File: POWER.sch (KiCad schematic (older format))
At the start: 42 parts, among them J6001 BATT1, J6002 BATT2_XT60, J6003 BATT2_JST, J6004 BATT4_CELL2, J6005 BATT4_CELL1, J6006 BATT5_CELL2, J6007 BATT5_CELL1, J6008 BATT3_JST, U6001 D24V50F5, U6002 D36V28F3, U6003 LM7809_TO220, U6004 D36V50F6, U6005 D36V50F6, U6006 D24V50F5

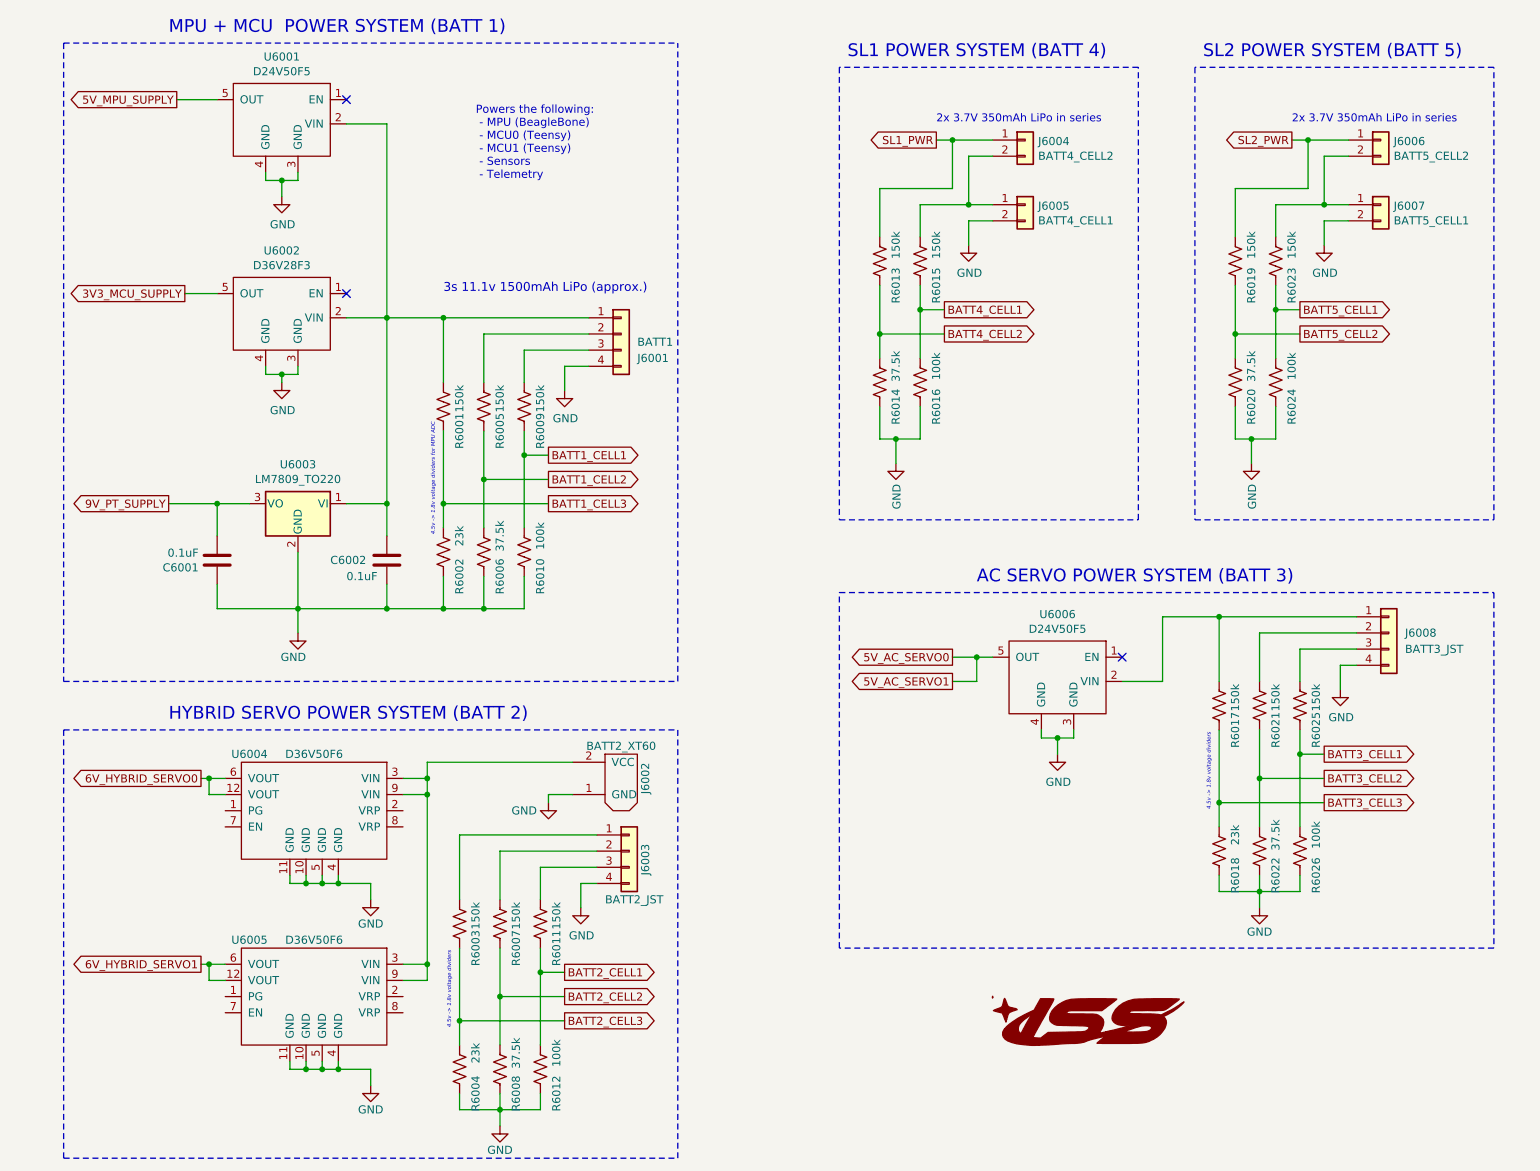
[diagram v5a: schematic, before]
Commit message: Fixed D36V28F3 footprint, made a Telemetrum footprint and symbol
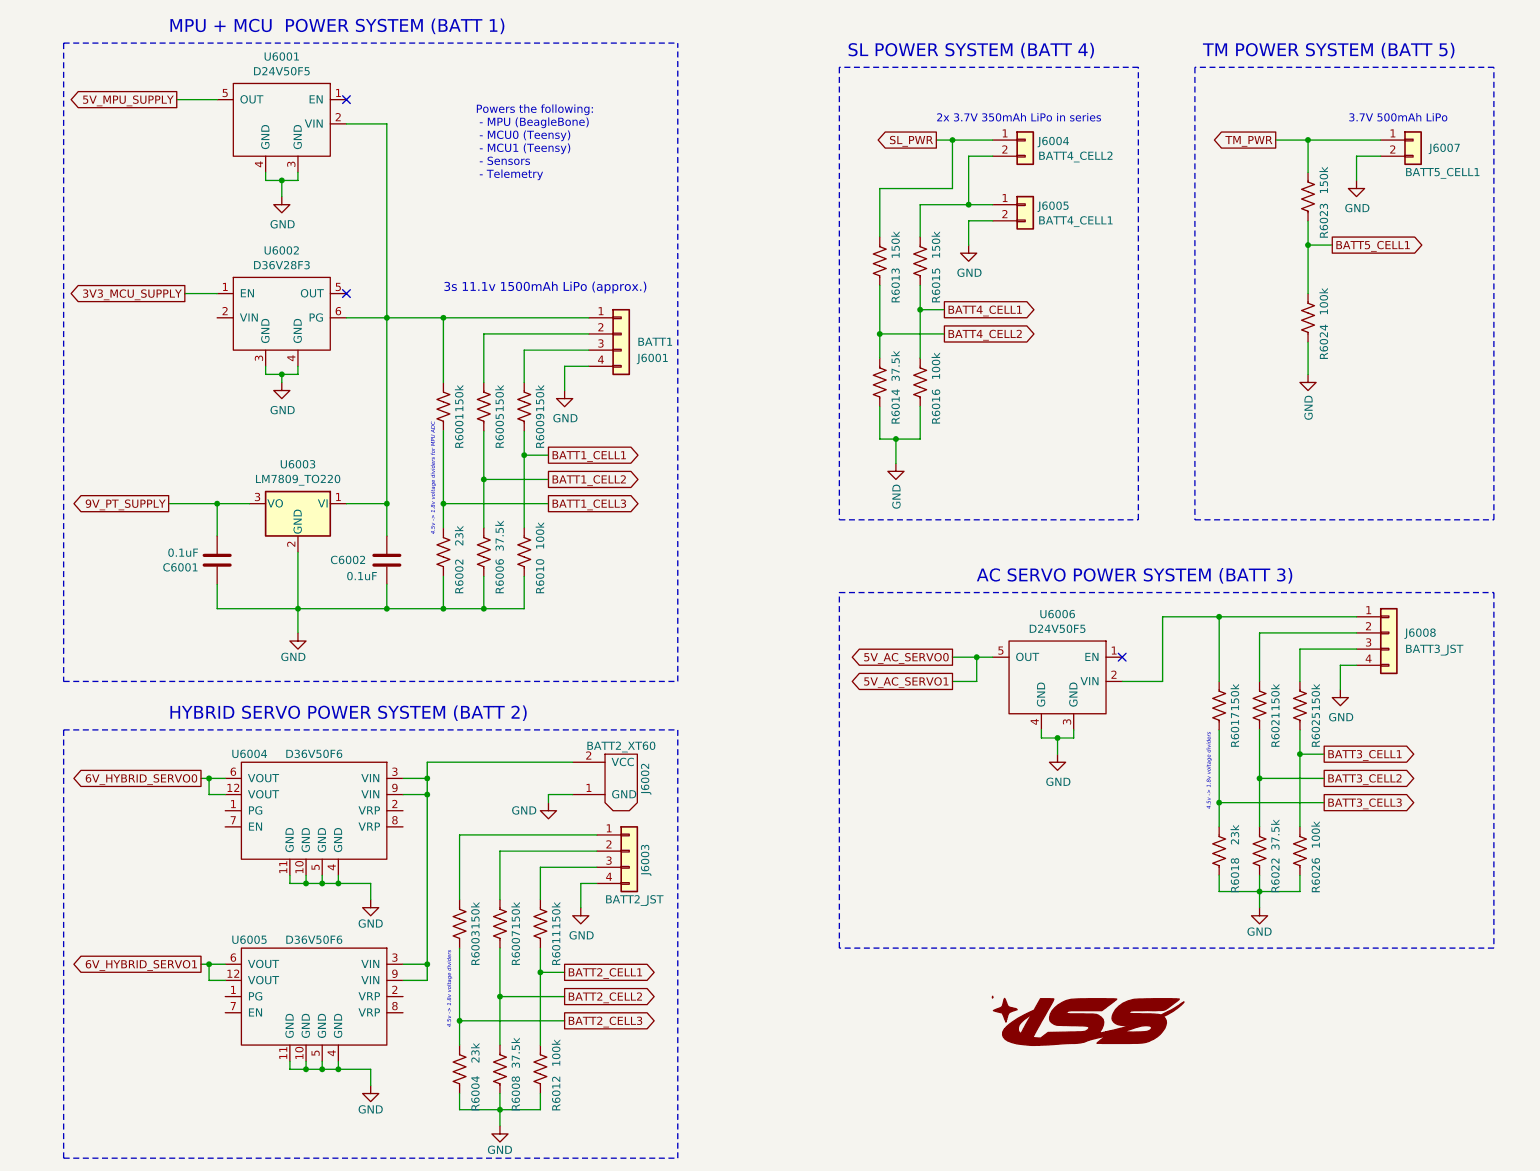
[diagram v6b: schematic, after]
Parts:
- removed J6006: BATT5_CELL2, Connector_JST:JST_PH_B2B-PH-K_1x02_P2.00mm_Vertical, symbol Connector_Generic:Conn_01x02
- removed R6019: 150k, symbol D24V50F5:R_US
- removed R6020: 37.5k, symbol D24V50F5:R_US
- removed U6002: D36V28F3, D24V50F5:D24V50F5, symbol D24V50F5:D24V50F5
- added U6002: D36V28F3, D36V28F3:D36V28F3, symbol D36V28F3:D36V28F3
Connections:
- net 3V3_MCU_SUPPLY: now also U6002.1 (EN)
- net GND: now also U6002.3 (GND), U6002.4 (GND)
- net at C6002.1, J6001.1 (Pin_1), R6001.2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: now also U6002.6 (PG)
- net TM_PWR: now reaches J6007.1 (Pin_1), R6023.2
- net SL1_PWR renamed SL_PWR
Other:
- note added: "3.7V 500mAh LiPo"
- note added: "SL POWER SYSTEM (BATT 4)"
- note added: "TM POWER SYSTEM (BATT 5)"
- note removed: "SL1 POWER SYSTEM (BATT 4)"
- note removed: "SL2 POWER SYSTEM (BATT 5)"
- moved on the sheet: J6007, R6023, R6024
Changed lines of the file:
@@
 	7900 3700 7900 900
-$Comp
-L Connector_Generic:Conn_01x02 J6007
-U 1 1 5FF794E5
-P 9400 1750
-F 0 "J6007" H 9480 1742 50  0000 L CNN
-F 1 "BATT5_CELL1" H 9480 1651 50  0000 L CNN
-F 2 "Connector_JST:JST_PH_B2B-PH-K_1x02_P2.00mm_Vertical" H 9400 1750 50  0001 C CNN
-F 3 "~" H 9400 1750 50  0001 C CNN
-	1    9400 1750
-	1    0    0    -1
-$EndComp
-$Comp
-L Connector_Generic:Conn_01x02 J6006
-U 1 1 5FF794EB
-P 9400 1350
-F 0 "J6006" H 9480 1342 50  0000 L CNN
-F 1 "BATT5_CELL2" H 9480 1251 50  0000 L CNN
-F 2 "Connector_JST:JST_PH_B2B-PH-K_1x02_P2.00mm_Vertical" H 9400 1350 50  0001 C CNN
-F 3 "~" H 9400 1350 50  0001 C CNN
-	1    9400 1350
-	1    0    0    -1
-$EndComp
 $Comp
 L power:GND #PWR06015
 U 1 1 5FF794F1
-P 9050 2000
-F 0 "#PWR06015" H 9050 1750 50  0001 C CNN
-F 1 "GND" H 9055 1827 50  0000 C CNN
-F 2 "" H 9050 2000 50  0001 C CNN
-F 3 "" H 9050 2000 50  0001 C CNN
-	1    9050 2000
-	1    0    0    -1
-$EndComp
-Wire Wire Line
-	9200 1450 9050 1450
-Wire Wire Line
-	9200 1850 9050 1850
-Wire Wire Line
-	9050 2000 9050 1850
-Text GLabel 8900 2400 2    50   Output ~ 0
+P 9250 1600
+F 0 "#PWR06015" H 9250 1350 50  0001 C CNN
+F 1 "GND" H 9255 1427 50  0000 C CNN
+F 2 "" H 9250 1600 50  0001 C CNN
+F 3 "" H 9250 1600 50  0001 C CNN
+	1    9250 1600
+	1    0    0    -1
+$EndComp
+Wire Wire Line
+	9400 1450 9250 1450
+Wire Wire Line
+	9250 1600 9250 1450
+Text GLabel 9100 2000 2    50   Output ~ 0
 BATT5_CELL1
-Text GLabel 8900 2550 2    50   Output ~ 0
-BATT5_CELL2
 $Comp
 L D24V50F5:R_US R6023
 U 1 1 5FF794FD
-P 8750 2100
-F 0 "R6023" V 8650 2250 50  0000 C CNN
-F 1 "150k" V 8650 2000 50  0000 C CNN
-F 2 "" V 8790 2090 50  0001 C CNN
-F 3 "~" H 8750 2100 50  0001 C CNN
-	1    8750 2100
-	-1   0    0    1
-$EndComp
-$Comp
-L D24V50F5:R_US R6019
-U 1 1 5FF79503
-P 8500 2100
-F 0 "R6019" V 8400 2250 50  0000 C CNN
-F 1 "150k" V 8400 2000 50  0000 C CNN
-F 2 "" V 8540 2090 50  0001 C CNN
-F 3 "~" H 8500 2100 50  0001 C CNN
-	1    8500 2100
-	-1   0    0    1
-$EndComp
-Wire Wire Line
-	8750 1950 8750 1750
-Wire Wire Line
-	8750 2250 8750 2400
-Wire Wire Line
-	8750 2400 8900 2400
-Wire Wire Line
-	8500 2250 8500 2550
-Wire Wire Line
-	8500 2550 8900 2550
+P 8950 1700
+F 0 "R6023" V 8850 1850 50  0000 C CNN
+F 1 "150k" V 8850 1600 50  0000 C CNN
+F 2 "" V 8990 1690 50  0001 C CNN
+F 3 "~" H 8950 1700 50  0001 C CNN
+	1    8950 1700
+	-1   0    0    1
+$EndComp
+Wire Wire Line
+	8950 1550 8950 1350
+Wire Wire Line
+	8950 1850 8950 2000
+Wire Wire Line
+	8950 2000 9100 2000
 $Comp
 L D24V50F5:R_US R6024
 U 1 1 5FF7950E
-P 8750 2850
-F 0 "R6024" V 8650 3000 50  0000 C CNN
-F 1 "100k" V 8650 2750 50  0000 C CNN
-F 2 "" V 8790 2840 50  0001 C CNN
-F 3 "~" H 8750 2850 50  0001 C CNN
-	1    8750 2850
-	-1   0    0    1
-$EndComp
-$Comp
-L D24V50F5:R_US R6020
-U 1 1 5FF79514
-P 8500 2850
-F 0 "R6020" V 8400 3000 50  0000 C CNN
-F 1 "37.5k" V 8400 2750 50  0000 C CNN
-F 2 "" V 8540 2840 50  0001 C CNN
-F 3 "~" H 8500 2850 50  0001 C CNN
-	1    8500 2850
-	-1   0    0    1
-$EndComp
-Wire Wire Line
-	8750 3200 8750 3000
-Wire Wire Line
-	8500 3000 8500 3200
-Wire Wire Line
-	8500 3200 8600 3200
-Wire Wire Line
-	8750 1750 9050 1750
-Wire Wire Line
-	9050 1750 9050 1450
-Connection ~ 9050 1750
-Wire Wire Line
-	9050 1750 9200 1750
-Wire Wire Line
-	8600 3200 8600 3350
+P 8950 2450
+F 0 "R6024" V 8850 2600 50  0000 C CNN
+F 1 "100k" V 8850 2350 50  0000 C CNN
+F 2 "" V 8990 2440 50  0001 C CNN
+F 3 "~" H 8950 2450 50  0001 C CNN
+	1    8950 2450
+	-1   0    0    1
+$EndComp
+Wire Wire Line
+	8950 2800 8950 2600
 $Comp
 L power:GND #PWR06013
 U 1 1 5FF79524
-P 8600 3350
-F 0 "#PWR06013" H 8600 3100 50  0001 C CNN
-F 1 "GND" V 8605 3222 50  0000 R CNN
-F 2 "" H 8600 3350 50  0001 C CNN
-F 3 "" H 8600 3350 50  0001 C CNN
-	1    8600 3350
-	1    0    0    -1
-$EndComp
-Connection ~ 8600 3200
-Wire Wire Line
-	8600 3200 8750 3200
-Wire Wire Line
-	8500 2700 8500 2550
-Connection ~ 8500 2550
-Wire Wire Line
-	8750 2700 8750 2400
-Connection ~ 8750 2400
+P 8950 2800
+F 0 "#PWR06013" H 8950 2550 50  0001 C CNN
+F 1 "GND" V 8955 2672 50  0000 R CNN
+F 2 "" H 8950 2800 50  0001 C CNN
+F 3 "" H 8950 2800 50  0001 C CNN
+	1    8950 2800
+	1    0    0    -1
+$EndComp
+Wire Wire Line
+	8950 2300 8950 2000
+Connection ~ 8950 2000
 Wire Notes Line
 	8250 900  8250 3700
@@
 Wire Notes Line
 	10100 900  8250 900
-Text Notes 8850 1250 0    49   ~ 0
-2x 3.7V 350mAh LiPo in series
+Text Notes 9200 1250 0    49   ~ 0
+3.7V 500mAh LiPo
 $Comp
 L D24V50F5:R_US R6016
@@
 $EndComp
 Text GLabel 6650 1350 0    50   Output ~ 0
-SL1_PWR
+SL_PWR
 Wire Wire Line
 	6750 1350 7000 1350
@@
 Wire Wire Line
 	6750 1350 6750 1650
-Text GLabel 8850 1350 0    50   Output ~ 0
-SL2_PWR
-Wire Wire Line
-	8950 1350 9200 1350
-Wire Wire Line
-	8850 1350 8950 1350
-Connection ~ 8950 1350
-Wire Wire Line
-	8500 1950 8500 1650
-Wire Wire Line
-	8500 1650 8950 1650
-Wire Wire Line
-	8950 1350 8950 1650
+Text GLabel 8750 1350 0    50   Output ~ 0
+TM_PWR
 Text Notes 8300 850  0    79   ~ 0
-SL2 POWER SYSTEM (BATT 5)
+TM POWER SYSTEM (BATT 5)
 $Comp
 L D24V50F5:D24V50F5 U6006
@@
 $EndComp
 $Comp
-L D24V50F5:D24V50F5 U6002
-U 1 1 5F963FAF
-P 2600 2150
-F 0 "U6002" H 2600 2265 50  0000 C CNN
-F 1 "D36V28F3" H 2600 2174 50  0000 C CNN
-F 2 "D24V50F5:D24V50F5" H 2600 2150 50  0001 C CNN
-F 3 "" H 2600 2150 50  0001 C CNN
-	1    2600 2150
-	-1   0    0    -1
-$EndComp
-$Comp
 L power:GND #PWR06001
 U 1 1 5F9641AC
@@
 	4350 6800 3700 6800
 Text Notes 6100 850  0    79   ~ 0
-SL1 POWER SYSTEM (BATT 4)
+SL POWER SYSTEM (BATT 4)
 Wire Notes Line
 	7900 900  6050 900
@@
 Text Notes 3800 1600 0    50   ~ 0
 Powers the following:\n - MPU (BeagleBone)\n - MCU0 (Teensy)\n - MCU1 (Teensy)\n - Sensors\n - Telemetry
+$Comp
+L D36V28F3:D36V28F3 U6002
+U 1 1 5FA400D5
+P 2600 2200
+F 0 "U6002" H 2600 2365 50  0000 C CNN
+F 1 "D36V28F3" H 2600 2274 50  0000 C CNN
+F 2 "D36V28F3:D36V28F3" H 3150 1700 50  0001 C CNN
+F 3 "" H 2600 2300 50  0001 C CNN
+	1    2600 2200
+	1    0    0    -1
+$EndComp
+$Comp
+L Connector_Generic:Conn_01x02 J6007
+U 1 1 5FF794E5
+P 9600 1350
+F 0 "J6007" H 9700 1300 50  0000 L CNN
+F 1 "BATT5_CELL1" H 9550 1150 50  0000 L CNN
+F 2 "Connector_JST:JST_PH_B2B-PH-K_1x02_P2.00mm_Vertical" H 9600 1350 50  0001 C CNN
+F 3 "~" H 9600 1350 50  0001 C CNN
+	1    9600 1350
+	1    0    0    -1
+$EndComp
+Wire Wire Line
+	8950 1350 9400 1350
+Connection ~ 8950 1350
+Wire Wire Line
+	8750 1350 8950 1350
 $EndSCHEMATC
